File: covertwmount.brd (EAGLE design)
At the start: 50.8 x 33.5 mm, 58 parts, among them J1 B2B-PH-K-S(LF)(SN), U1 STM32G081RBT6, U2 MMBT4401-7-F

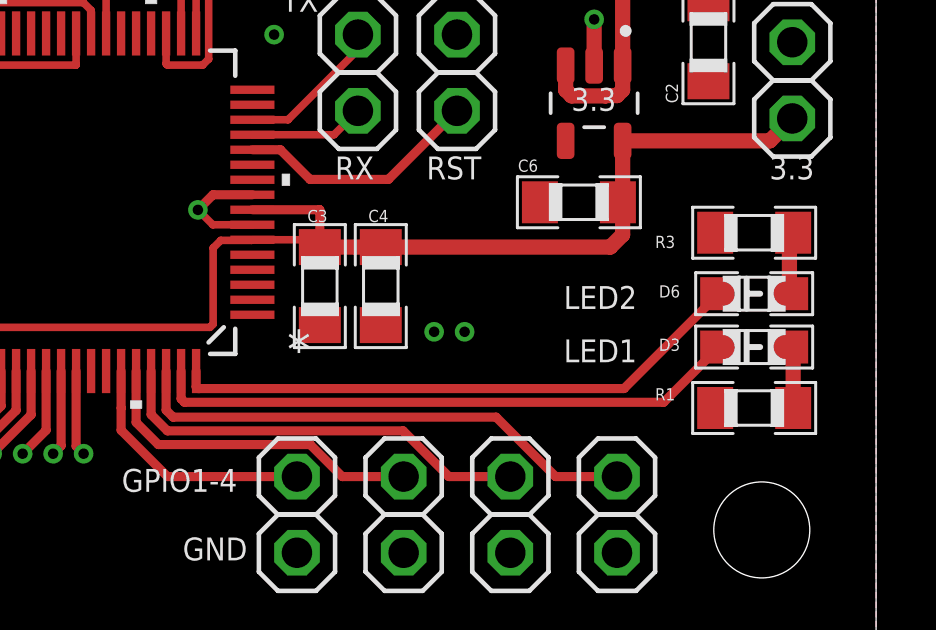
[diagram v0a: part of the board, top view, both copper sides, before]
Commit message: move leds2
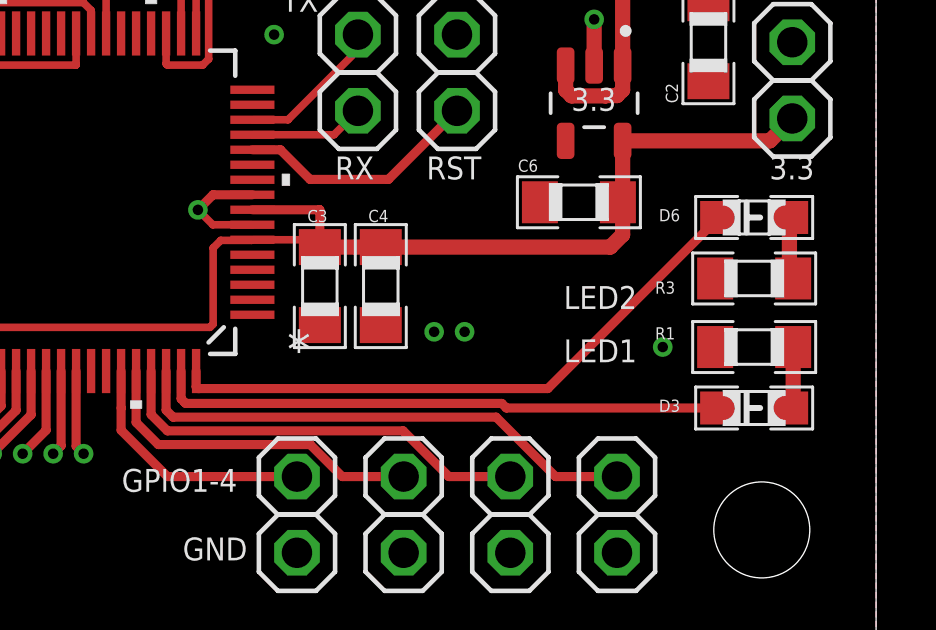
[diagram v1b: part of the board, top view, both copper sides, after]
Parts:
- moved D6 2.54 mm to (46.7, 14.0)
- moved D3 2.03 mm to (46.7, 7.62)
- moved R1 2.03 mm to (46.7, 9.65)
- moved R3 1.52 mm to (46.7, 11.9)
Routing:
- net GPIO_LED2: track 19.3 -> 20.3 mm
- net GPIO_LED1: track 19.7 -> 19.0 mm
- net GND: vias 31 -> 32
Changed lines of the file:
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@@
 <attribute name="VALUE" x="15.748" y="28.575" size="1.27" layer="27"/>
 </element>
-<element name="D6" library="standardparts" package="0805.LED" value="" x="46.736" y="11.43" smashed="yes">
-<attribute name="NAME" x="43.561" y="11.303" size="0.4064" layer="25" font="vector"/>
-<attribute name="VALUE" x="44.831" y="10.16" size="0.4064" layer="27" font="vector"/>
-</element>
-<element name="R3" library="standardparts" package="0805" value="500" x="46.736" y="13.462" smashed="yes">
-<attribute name="NAME" x="43.434" y="12.954" size="0.4064" layer="25" font="vector"/>
-<attribute name="VALUE" x="43.434" y="13.589" size="0.4064" layer="27" font="vector"/>
-</element>
-<element name="D3" library="standardparts" package="0805.LED" value="" x="46.736" y="9.652" smashed="yes">
-<attribute name="NAME" x="43.561" y="9.525" size="0.4064" layer="25" font="vector"/>
-<attribute name="VALUE" x="44.831" y="8.382" size="0.4064" layer="27" font="vector"/>
-</element>
-<element name="R1" library="standardparts" package="0805" value="500" x="46.736" y="7.62" smashed="yes">
-<attribute name="NAME" x="43.434" y="7.874" size="0.4064" layer="25" font="vector"/>
-<attribute name="VALUE" x="43.434" y="7.239" size="0.4064" layer="27" font="vector"/>
+<element name="D6" library="standardparts" package="0805.LED" value="" x="46.736" y="13.97" smashed="yes">
+<attribute name="NAME" x="43.561" y="13.843" size="0.4064" layer="25" font="vector"/>
+<attribute name="VALUE" x="44.831" y="12.7" size="0.4064" layer="27" font="vector"/>
+</element>
+<element name="R3" library="standardparts" package="0805" value="500" x="46.736" y="11.938" smashed="yes">
+<attribute name="NAME" x="43.434" y="11.43" size="0.4064" layer="25" font="vector"/>
+<attribute name="VALUE" x="43.434" y="12.065" size="0.4064" layer="27" font="vector"/>
+</element>
+<element name="D3" library="standardparts" package="0805.LED" value="" x="46.736" y="7.62" smashed="yes">
+<attribute name="NAME" x="43.561" y="7.493" size="0.4064" layer="25" font="vector"/>
+<attribute name="VALUE" x="44.831" y="6.35" size="0.4064" layer="27" font="vector"/>
+</element>
+<element name="R1" library="standardparts" package="0805" value="500" x="46.736" y="9.652" smashed="yes">
+<attribute name="NAME" x="43.434" y="9.906" size="0.4064" layer="25" font="vector"/>
+<attribute name="VALUE" x="43.434" y="9.271" size="0.4064" layer="27" font="vector"/>
 </element>
 <element name="S1" library="SparkFun-Switches" library_urn="urn:adsk.eagle:library:535" package="TACTILE_SWITCH_PTH_6.0MM" package3d_urn="urn:adsk.eagle:package:40163/1" value="MOMENTARY-SWITCH-SPST-PTH-6.0MM" x="11.43" y="29.21" smashed="yes">
@@
 <wire x1="30.0101" y1="14.728" x2="28.698" y2="14.728" width="0.3048" layer="1"/>
 <wire x1="28.698" y1="14.728" x2="28.194" y2="14.224" width="0.3048" layer="1"/>
+<via x="43.688" y="9.652" extent="1-16" drill="0.35"/>
 </signal>
 <signal name="SPI_SCK">
@@
 <wire x1="28.134" y1="8.8519" x2="28.134" y2="8.3277" width="0.3048" layer="1"/>
 <wire x1="28.134" y1="8.3277" x2="28.194" y2="8.2677" width="0.3048" layer="1"/>
-<wire x1="28.194" y1="8.2677" x2="42.3987" y2="8.2677" width="0.3048" layer="1"/>
-<wire x1="42.3987" y1="8.2677" x2="45.561" y2="11.43" width="0.3048" layer="1"/>
+<wire x1="28.194" y1="8.2677" x2="39.8587" y2="8.2677" width="0.3048" layer="1"/>
+<wire x1="39.8587" y1="8.2677" x2="45.561" y2="13.97" width="0.3048" layer="1"/>
 </signal>
 <signal name="RESET">
@@
 <contactref element="D6" pad="P$2"/>
 <contactref element="R3" pad="2"/>
-<wire x1="47.911" y1="11.43" x2="47.911" y2="13.337" width="0.508" layer="1"/>
-<wire x1="47.911" y1="13.337" x2="48.036" y2="13.462" width="0.508" layer="1"/>
+<wire x1="47.911" y1="13.97" x2="47.911" y2="12.063" width="0.508" layer="1"/>
+<wire x1="48.036" y1="11.938" x2="47.911" y2="12.063" width="0.508" layer="1"/>
 </signal>
 <signal name="N$3">
 <contactref element="D3" pad="P$2"/>
 <contactref element="R1" pad="2"/>
-<wire x1="47.911" y1="9.652" x2="48.036" y2="9.527" width="0.508" layer="1"/>
-<wire x1="48.036" y1="9.527" x2="48.036" y2="7.62" width="0.508" layer="1"/>
+<wire x1="48.036" y1="9.652" x2="48.036" y2="7.745" width="0.508" layer="1"/>
+<wire x1="48.036" y1="7.745" x2="47.911" y2="7.62" width="0.508" layer="1"/>
 </signal>
 <signal name="GPIO_LED1">
@@
 <contactref element="D3" pad="P$1"/>
 <wire x1="27.634" y1="8.8519" x2="27.634" y2="7.926" width="0.3048" layer="1"/>
-<wire x1="27.7495" y1="7.8105" x2="43.7195" y2="7.8105" width="0.3048" layer="1"/>
-<wire x1="43.7195" y1="7.8105" x2="45.561" y2="9.652" width="0.3048" layer="1"/>
 <wire x1="27.634" y1="7.926" x2="27.7495" y2="7.8105" width="0.3048" layer="1"/>
+<wire x1="27.7495" y1="7.8105" x2="27.7876" y2="7.7724" width="0.3048" layer="1"/>
+<wire x1="27.7876" y1="7.7724" x2="38.32486875" y2="7.7724" width="0.3048" layer="1"/>
+<wire x1="38.32486875" y1="7.7724" x2="38.47726875" y2="7.62" width="0.3048" layer="1"/>
+<wire x1="38.47726875" y1="7.62" x2="45.561" y2="7.62" width="0.3048" layer="1"/>
 </signal>
 <signal name="N$4">
